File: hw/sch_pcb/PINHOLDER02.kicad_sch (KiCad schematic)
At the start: 7 parts, among them J1 HEADER_1x03, M2 HOLE, M3 HOLE, M4 HOLE

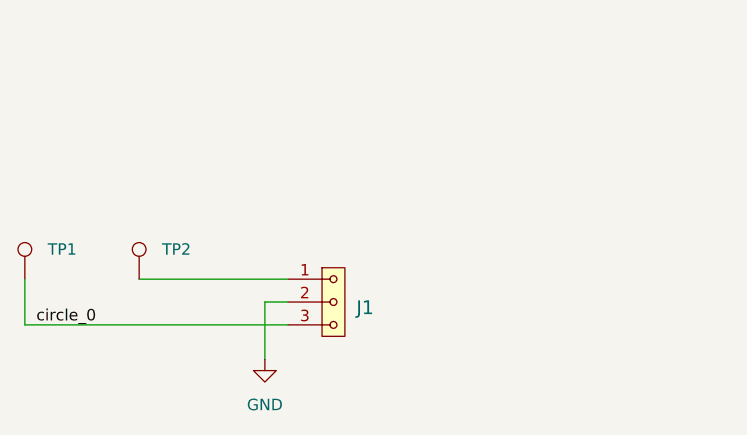
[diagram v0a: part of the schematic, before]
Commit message: zamena anoda-katoda
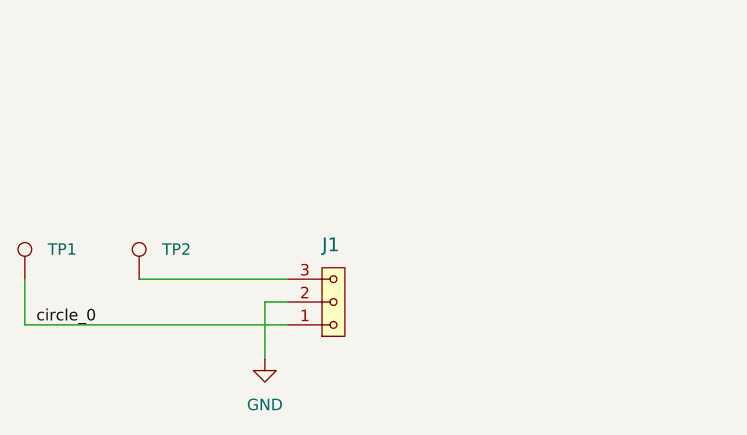
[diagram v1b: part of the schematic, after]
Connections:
- net circle_0: now also J1.1; no longer J1.3
- net at TP2.1: now also J1.3; no longer J1.1
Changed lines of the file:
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@@
     (pin "1")
   )
-  (symbol (lib_id "MLAB_HEADER:HEADER_1x03") (at 151.13 99.06 0) (unit 1)
-    (in_bom yes) (on_board yes) (fields_autoplaced)
-    (property "Reference" "J1" (id 0) (at 153.67 99.695 0)
+  (symbol (lib_id "MLAB_HEADER:HEADER_1x03") (at 151.13 99.06 0) (mirror x) (unit 1)
+    (in_bom yes) (on_board yes)
+    (property "Reference" "J1" (id 0) (at 149.86 92.71 0)
       (effects (font (size 1.524 1.524)) (justify left))
     )
-    (property "Value" "HEADER_1x03" (id 1) (at 153.67 101.6 0)
+    (property "Value" "HEADER_1x03" (id 1) (at 153.67 96.52 0)
       (effects (font (size 1.524 1.524)) (justify left) hide)
     )
-    (property "Footprint" "Connector_PinHeader_2.54mm:PinHeader_1x03_P2.54mm_Vertical_SMD_Pin1Left" (id 2) (at 151.13 96.52 0)
+    (property "Footprint" "Connector_PinHeader_2.54mm:PinHeader_1x03_P2.54mm_Vertical_SMD_Pin1Left" (id 2) (at 151.13 101.6 0)
       (effects (font (size 1.524 1.524)) hide)
     )
-    (property "Datasheet" "" (id 3) (at 151.13 96.52 0)
+    (property "Datasheet" "" (id 3) (at 151.13 101.6 0)
       (effects (font (size 1.524 1.524)))
     )

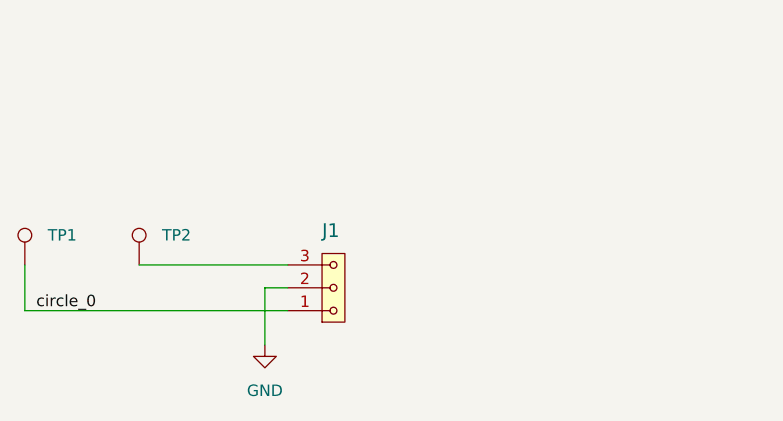
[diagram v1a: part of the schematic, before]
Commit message: schematics anotate
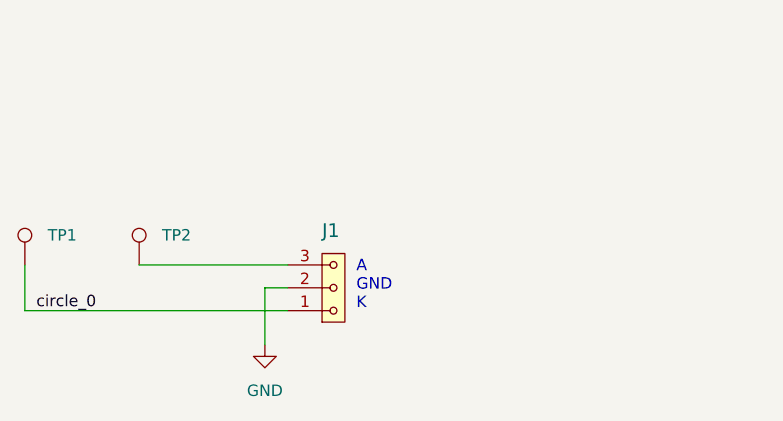
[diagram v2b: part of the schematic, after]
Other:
- note added: "A GND K"
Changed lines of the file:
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@@
     (effects (font (size 1.524 1.524)) (justify left bottom))
+  )
+  (text "A\nGND\nK" (at 153.67 101.6 0)
+    (effects (font (size 1.27 1.27)) (justify left bottom))
   )
   (label "circle_0" (at 118.11 101.6 0)
